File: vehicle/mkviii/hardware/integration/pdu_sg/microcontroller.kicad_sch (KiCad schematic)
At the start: 15 parts, among them J1 J_Programming_Pin_Header, U1 STM32G441KBT6, U2 MCP2561-E_SN, Y1 X_16MHz_18pF

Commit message: GPIO pins done
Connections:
- net HB_LED: now also U1.30 ((TIM3_CH4/TIM4_CH2/TIM17_CH1N/GPIO_EXTI7)PB7)
- net SS_ESTOP_R: now reaches U1.10 ((TIM2_ETR/TIM2_CH1/GPIO_EXTI5/ADC2_IN13)PA5*)
- net SCK: now reaches U1.26 ((TIM3_ETR/SPI1_SCK/TIM4_ETR/TIM2_CH2/GPIO_EXTI3)PB3)
- net COOLING_EN: now reaches U1.29 ((TIM4_CH1/TIM16_CH1N/GPIO_EXTI6)PB6)
- net RESET: now reaches U1.31 ((TIM4_CH3/TIM16_CH1/GPIO_EXTI8)PB8-BOOT0)
- net SS_MC: now reaches U1.7 ((TIM15_CH1/USART2_TX/TIM2_CH3/GPIO_EXTI2/ADC1_IN3)PA2*)
- net SS_GLVMS: now reaches U1.8 ((TIM15_CH2/USART2_RX/TIM2_CH4/GPIO_EXTI3/ADC1_IN4)PA3*)
- net SS_ESTOP_L: now reaches U1.9 ((USART2_CK/TIM3_CH2/GPIO_EXTI4/ADC2_IN17)PA4*)
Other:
- note added: "Flashing"
- note added: "Heartbeat LED"
- moved on the sheet: C7, C8, D1, R1, Y1

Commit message: fix in/out + TS_STATUS_*
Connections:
- net SS_ESTOP_R: now also U1.8 ((TIM15_CH2/USART2_RX/TIM2_CH4/GPIO_EXTI3/ADC1_IN4)PA3*); no longer U1.10 ((TIM2_ETR/TIM2_CH1/GPIO_EXTI5/ADC2_IN13)PA5*)
- net SS_GLVMS: now also U1.7 ((TIM15_CH1/USART2_TX/TIM2_CH3/GPIO_EXTI2/ADC1_IN3)PA2*); no longer U1.8 ((TIM15_CH2/USART2_RX/TIM2_CH4/GPIO_EXTI3/ADC1_IN4)PA3*)
- net SS_MC: now also U1.6 ((TIM15_CH1N/TIM2_CH2/GPIO_EXTI1/ADC2_IN2/ADC1_IN2)PA1*); no longer U1.7 ((TIM15_CH1/USART2_TX/TIM2_CH3/GPIO_EXTI2/ADC1_IN3)PA2*)
- net TS_STATUS_G: now reaches U1.12 ((TIM3_CH2/TIM17_CH1/GPIO_EXTI7/ADC2_IN4)PA7*)
- new net TS_STATUS_R: U1.10 ((TIM2_ETR/TIM2_CH1/GPIO_EXTI5/ADC2_IN13)PA5*)
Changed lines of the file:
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@@
 	)
 	(hierarchical_label "COOLING_EN"
-		(shape input)
+		(shape output)
 		(at 149.86 96.52 0)
 		(effects
@@
 	)
 	(hierarchical_label "FAN_PWM"
-		(shape input)
+		(shape output)
 		(at 149.86 68.58 0)
 		(effects
@@
 	)
 	(hierarchical_label "PUMP_PWM"
-		(shape input)
+		(shape output)
 		(at 149.86 53.34 0)
 		(effects
@@
 	(hierarchical_label "SS_GLVMS"
 		(shape input)
-		(at 149.86 60.96 0)
+		(at 149.86 58.42 0)
+		(effects
+			(font
+				(size 1.27 1.27)
+			)
+			(justify left)
+		)
+	)
+	(hierarchical_label "TS_STATUS_R"
+		(shape output)
+		(at 149.86 66.04 0)
+		(effects
+			(font
+				(size 1.27 1.27)
+			)
+			(justify left)
+		)
+	)
+	(hierarchical_label "TS_STATUS_G"
+		(shape output)
+		(at 149.86 71.12 0)
 		(effects
 			(font
@@
 	(hierarchical_label "SS_MC"
 		(shape input)
-		(at 149.86 58.42 0)
+		(at 149.86 55.88 0)
 		(effects
 			(font
@@
 	(hierarchical_label "SS_ESTOP_R"
 		(shape input)
-		(at 149.86 66.04 0)
+		(at 149.86 60.96 0)
 		(effects
 			(font

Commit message: reorganizing
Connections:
- net +3.3V is gone; now on net +3V3: C1.1, C2.1, C3.1, U1.1 (VDD), U1.17 (VDD)
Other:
- moved on the sheet: C9, U2

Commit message: adc
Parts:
- added C22, C23, C24, C25, C26, C27, C28, C29: C_10uF, OEM:C_0603, symbol OEM:C_10uF
- added C30: C_10uF, OEM:C_0603_1608Metric, symbol OEM:C_10uF_10V_0603
- added R18, R20, R45, R54, R55, R56, R57, R58, R59: R_1K, OEM:R_0603, symbol OEM:R_1K
- added U20: ADC1283, Package_SO:TSSOP-16_4.4x5mm_P0.65mm, symbol Analog_ADC:ADC1283
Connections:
- net +5V: now also C30.1, R45.1, U20.13 (DVCC), U20.2 (AVCC)
- net GND: now also C22.2, C23.2, C24.2, C25.2, C26.2, C27.2, C28.2, C29.2, C30.2, U20.12 (DGND), U20.3 (AGND)
- net MISO: now also U20.15 (DOUT)
- net MOSI: now also U20.14 (DIN)
- net SCK: now also U20.16 (SCLK)
- new net: C25.1, R55.2, U20.7 (IN3)
- new net: C24.1, R54.2, U20.6 (IN2)
- new net: C27.1, R58.2, U20.10 (IN6)
- new net: C26.1, R59.2, U20.11 (IN7)
- new net: C22.1, R18.2, U20.4 (IN0)
- new net: C23.1, R20.2, U20.5 (IN1)
- new net: C29.1, R56.2, U20.8 (IN4)
- new net: C28.1, R57.2, U20.9 (IN5)
- new net A_COOLING: R18.1
- new net A_LV_MOBO: R55.1
- new net A_MC: R54.1
- new net A_PDU: R59.1
- new net A_SHDN: R58.1
- new net A_SS: R20.1
- new net CS_ADC: U20.1 (~{CS})
- new net SIG_TEMP: R57.1
- new net V_SENSE: R45.2, R56.1
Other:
- note added: "ADC"
- moved on the sheet: C1, C2, C3, C4, C5, C6, C7, C8, D1, J1, R1, U1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

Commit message: L- P- display
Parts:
- added R19: R_10k, OEM:R_0603_1608Metric, symbol OEM:R_10k_0.1W_0603
- added U11: CA56-12SEKWA, Display_7Segment:CA56-12SEKWA, symbol Display_Character:CA56-12SEKWA
- added U12: MAX7221xNG, Package_DIP:DIP-24_W7.62mm, symbol Driver_LED:MAX7221xNG
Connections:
- net +5V: now also R19.1, U12.19 (V+)
- net CS_ADC: now also U1.18 ((TIM4_ETR/USART1_CK/GPIO_EXTI8)PA8)
- net MOSI: now also U12.1 (DIN)
- net CS_DISP: now reaches U1.19 ((TIM2_CH3/TIM15_BKIN/USART1_TX/GPIO_EXTI9)PA9)
- net CS_DISP: now also U12.12 (~{CS})
- net CS_IO: now reaches U1.20 ((TIM2_CH4/USART1_RX/TIM17_BKIN/GPIO_EXTI10)PA10)
- net SCK: no longer names the net of U1.26 ((TIM3_ETR/SPI1_SCK/TIM4_ETR/TIM2_CH2/GPIO_EXTI3)PB3), U20.16 (SCLK)
- net SCK: now also U12.13 (CLK)
- new net: U11.1 (e), U12.21 (SEG_E)
- new net: U11.10 (f), U12.15 (SEG_F)
- new net: U11.11 (a), U12.14 (SEG_A)
- new net: U11.2 (d), U12.23 (SEG_D)
- new net: U11.3 (DPX), U12.22 (SEG_DP)
- new net: U11.4 (c), U12.20 (SEG_C)
- new net: U11.5 (g), U12.17 (SEG_G)
- new net: U11.7 (b), U12.16 (SEG_B)
- new net: R19.2, U12.18 (ISET)
- new net: U12.4 (GND), U12.9 (GND)
- new net DIG_0: U11.12 (CA1), U12.2 (DIG_0)
- new net DIG_1: U11.9 (CA2), U12.11 (DIG_1)
- new net DIG_2: U11.8 (CA3), U12.6 (DIG_2)
- new net DIG_3: U11.6 (CA4), U12.7 (DIG_3)
- no-connect marks 1 -> 8
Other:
- moved on the sheet: C9, U2

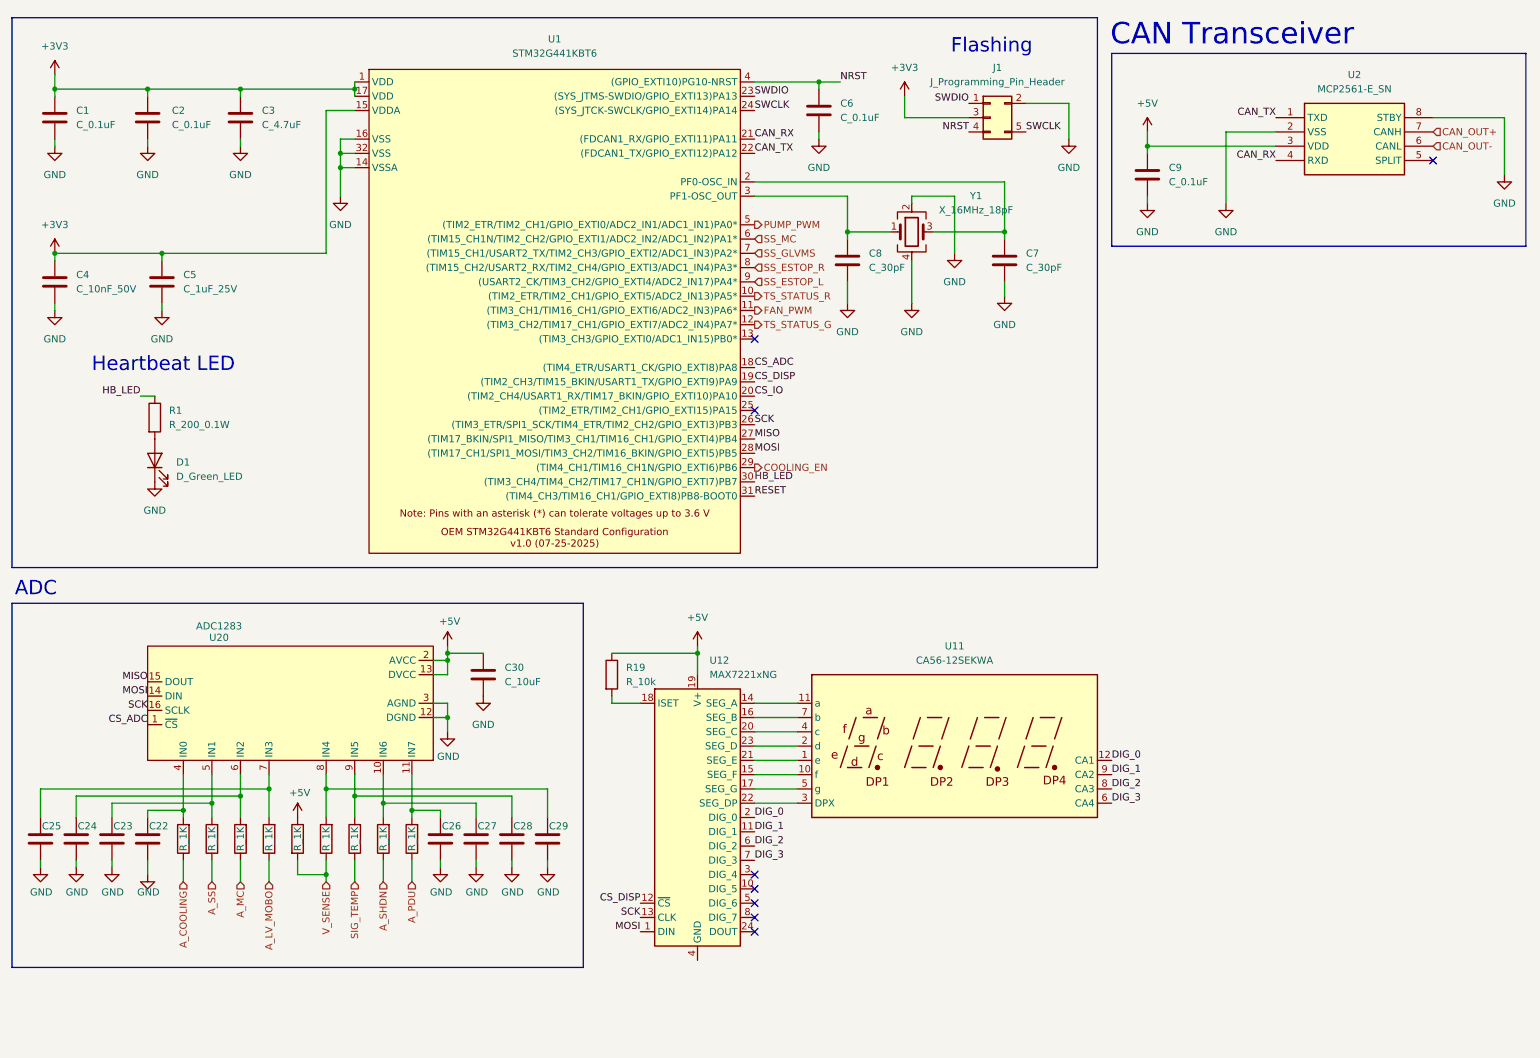
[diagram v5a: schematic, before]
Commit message: shutdown node leds
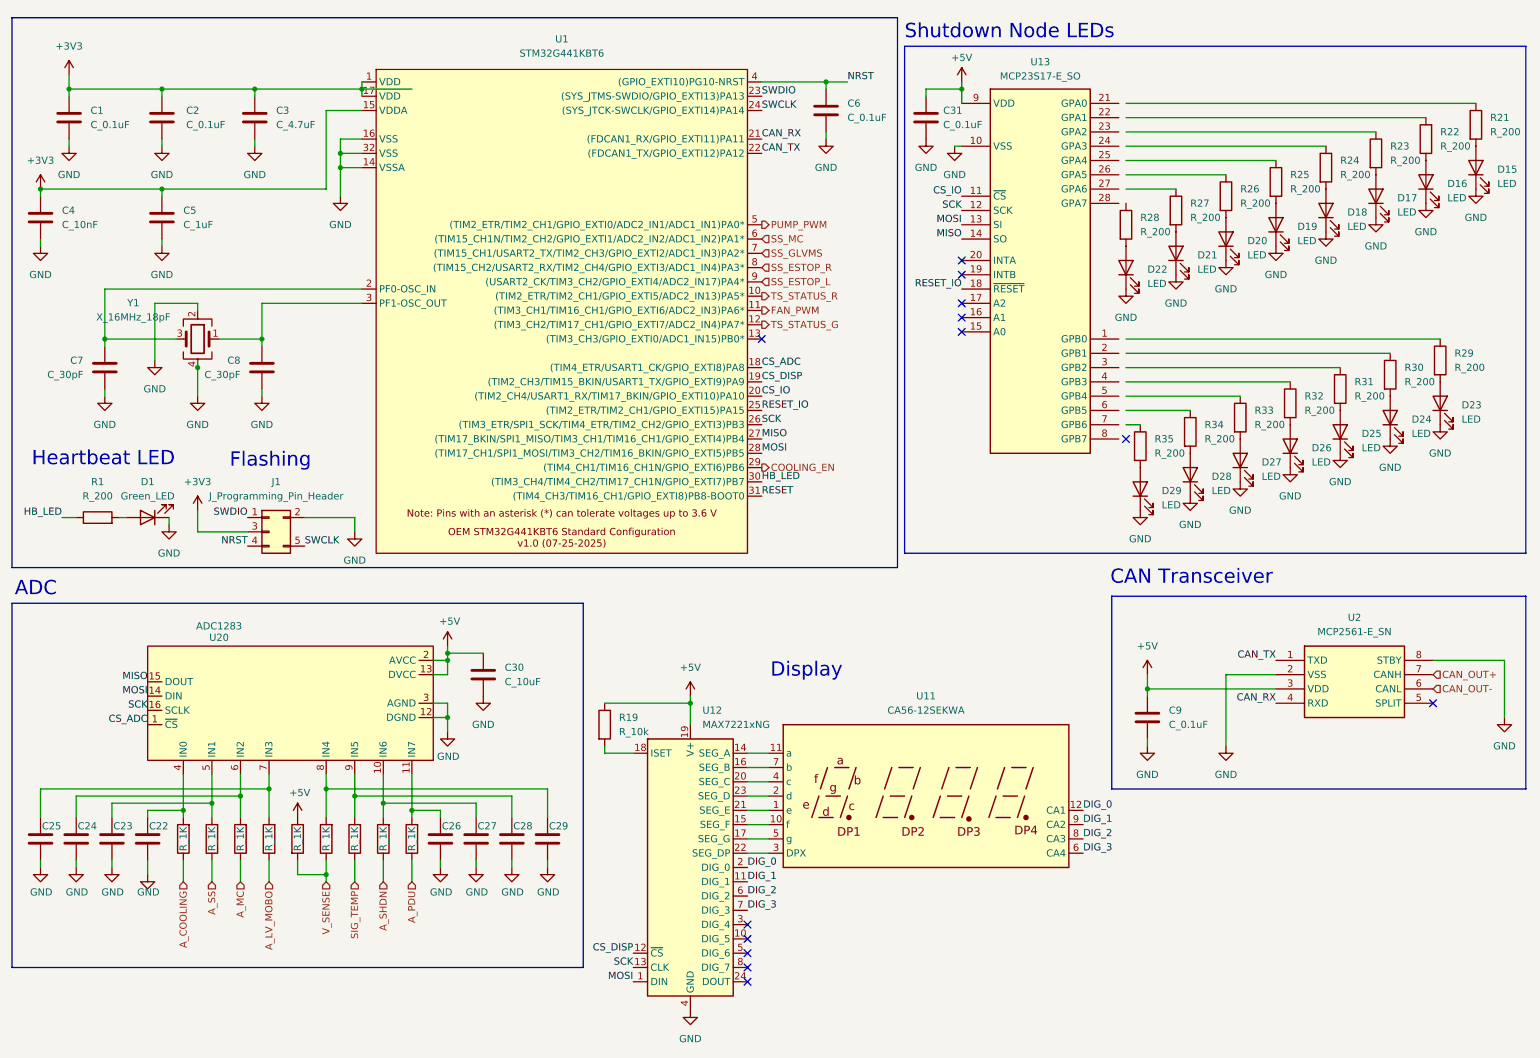
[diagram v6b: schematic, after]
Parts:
- added C31: C_0.1uF, OEM:C_0603_1608Metric, symbol OEM:C_0.1uF_16V_0603
- added D15, D16, D17, D18, D19, D20, D21, D22, D23, D24, D25, D26, D27, D28, D29: LED, OEM:D_0805_2012Metric, symbol OEM:D_LED_White_0805
- added R21, R22, R23, R24, R25, R26, R27, R28, R29, R30, R31, R32, R33, R34, R35: R_200, OEM:R_0603_1608Metric, symbol OEM:R_200_0.1W_0603
- added U13: MCP23S17-E_SO, OEM:U_SPI-IO-Xpndr_MCP23S17-E_SO_SOIC-28, symbol OEM:U_SPI-IO-Xpndr_MCP23S17-E_SO_SOIC-28
- C4: value C_10nF_50V -> C_10nF
- C5: value C_1uF_25V -> C_1uF
- D1: value D_Green_LED -> Green_LED
- R1: value R_200_0.1W -> R_200
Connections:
- net +5V: now also C31.1, U13.9 (VDD)
- net CS_IO: now also U13.11 (~{CS})
- net GND: now also U12.4 (GND), U12.9 (GND), C31.2, D15.1 (K), D16.1 (K), D17.1 (K), D18.1 (K), D19.1 (K), D20.1 (K), D21.1 (K), D22.1 (K), D23.1 (K), D24.1 (K), D25.1 (K), D26.1 (K), D27.1 (K), D28.1 (K), D29.1 (K), U13.10 (VSS)
- net MISO: now also U13.14 (SO)
- net MOSI: now also U13.13 (SI)
- net at U1.26 ((TIM3_ETR/SPI1_SCK/TIM4_ETR/TIM2_CH2/GPIO_EXTI3)PB3), U12.13 (CLK), U20.16 (SCLK): now also U13.12 (SCK)
- net RESET_IO: now reaches U1.25 ((TIM2_ETR/TIM2_CH1/GPIO_EXTI15)PA15)
- net RESET_IO: now also U13.18 (~{RESET})
- new net: D24.2 (A), R30.2
- new net: D29.2 (A), R35.2
- new net: D22.2 (A), R28.2
- new net: D27.2 (A), R33.2
- new net: D21.2 (A), R27.2
- new net: D15.2 (A), R21.2
- new net: D25.2 (A), R31.2
- new net: D28.2 (A), R34.2
- new net: D20.2 (A), R26.2
- new net: D17.2 (A), R23.2
- new net: D26.2 (A), R32.2
- new net: D18.2 (A), R24.2
- new net: D23.2 (A), R29.2
- new net: D16.2 (A), R22.1
- new net: D19.2 (A), R25.2
- no-connect marks 8 -> 13
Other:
- note added: "Display"
- note added: "Shutdown Node LEDs"
- moved on the sheet: C1, C2, C3, C4, C5, C6, C7, C8, C9, D1, J1, R1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

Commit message: fix symbols after changing library
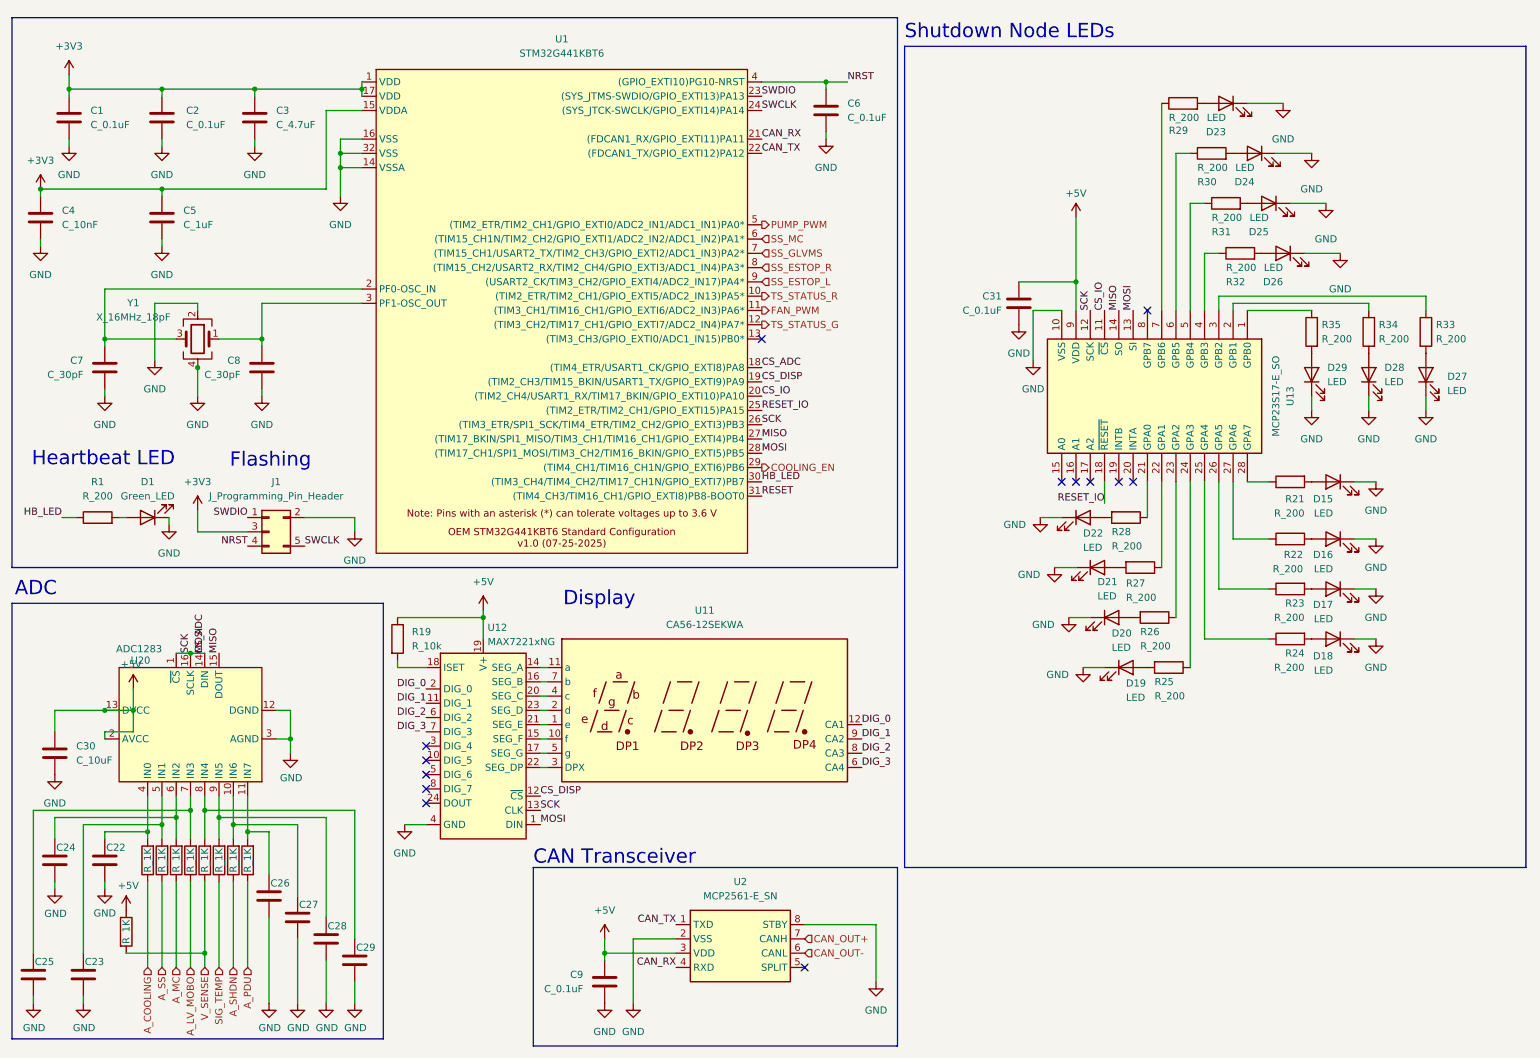
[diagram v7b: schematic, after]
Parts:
- C22, C23, C24, C25, C26, C27, C28, C29: footprint OEM:C_0603 -> Capacitor_SMD:C_0603_1608Metric
- D1, D15, D16, D17, D18, D19, D20, D21, D22, D23, D24, D25, D26, D27, D28, D29: footprint OEM:D_0805_2012Metric -> Diode_SMD:D_0805_2012Metric
- R1, R19, R21, R22, R23, R24, R25, R26, R27, R28, R29, R30, R31, R32, R33, R34, R35: footprint OEM:R_0603_1608Metric -> Resistor_SMD:R_0603_1608Metric
- U1: footprint OEM:LQFP-32_7x7mm_P0.8mm -> Package_QFP:LQFP-32_7x7mm_P0.8mm
- U2: footprint OEM:SOIC-8_3.9x4.9mm_P1.27mm -> Package_SO:SOIC-8_3.9x4.9mm_P1.27mm
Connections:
- net MOSI is gone; now on net CS_ADC: U1.28 ((TIM17_CH1/SPI1_MOSI/TIM3_CH2/TIM16_BKIN/GPIO_EXTI5)PB5), U12.1 (DIN), U13.13 (SI), U20.14 (DIN)
- net CS_ADC: now also U1.26 ((TIM3_ETR/SPI1_SCK/TIM4_ETR/TIM2_CH2/GPIO_EXTI3)PB3), U12.13 (CLK), U13.12 (SCK), U20.16 (SCLK)
- net GND: no longer U12.9 (GND)
- net at R35.1: now also U13.1 (GPB0)
- net at R27.1: now also U13.22 (GPA1)
- net at R21.1: now also U13.28 (GPA7)
- net at R31.1: now also U13.5 (GPB4)
- net at R26.1: now also U13.23 (GPA2)
- net at U13.2 (GPB1): now also R34.1
- net at U13.21 (GPA0): now also R28.1
- net at U13.24 (GPA3): now also R25.1
- net at U13.25 (GPA4): now also R24.1
- net at U13.26 (GPA5): now also R23.1
- net at U13.27 (GPA6): now also R22.2
- net at U13.3 (GPB2): now also R33.1
- net at U13.4 (GPB3): now also R32.1
- net at U13.6 (GPB5): now also R30.1
- net at U13.7 (GPB6): now also R29.1
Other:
- moved on the sheet: C22, C23, C24, C25, C26, C27, C28, C29, C30, C31, C9, D15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
